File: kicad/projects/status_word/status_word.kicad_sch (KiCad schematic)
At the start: 9 parts, among them J1 peripheral_addr_bus_connector, J2 peripheral_aux_connector, J3 peripheral_membank_connector

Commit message: WIP on status word
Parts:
- added C2, C3, C4, C5, C6, C7: C, Capacitor_THT:C_Disc_D5.0mm_W2.5mm_P5.00mm, symbol Device:C
- added D1, D10, D11, D12, D13, D14, D15, D16, D2, D3, D4, D5, D6, D7, D8, D9: LED, sixteen-bit-computer:LED_D5.0mm_Horizontal_O3.81mm_Z3.0mm, symbol Device:LED
- added J10, J11, J12, J13, J6, J7, J8, J9: Conn_01x02_Pin, Connector_PinHeader_2.54mm:PinHeader_1x02_P2.54mm_Vertical, symbol Connector:Conn_01x02_Pin
- added J14: Conn_01x08_Socket, Connector_PinSocket_2.54mm:PinSocket_1x08_P2.54mm_Horizontal, symbol Connector:Conn_01x08_Socket
- added J4: Conn_01x16_Socket, Connector_PinSocket_2.54mm:PinSocket_1x16_P2.54mm_Horizontal, symbol Connector:Conn_01x16_Socket
- added J5: Conn_01x04_Socket, Connector_PinSocket_2.54mm:PinSocket_1x04_P2.54mm_Horizontal, symbol Connector:Conn_01x04_Socket
- added RN1, RN2, RN3: R_Network08_US, Resistor_THT:R_Array_SIP9, symbol Device:R_Network08_US
- added U1: 74HC10, Package_DIP:DIP-14_W7.62mm_Socket, symbol sixteen-bit-computer:74HC10
- added U2, U3: 74HC377, Package_DIP:DIP-20_W7.62mm_Socket, symbol sixteen-bit-computer:74HC377
- added U4, U5, U6, U7: 74HC245, Package_DIP:DIP-20_W7.62mm_Socket, symbol sixteen-bit-computer:74HC245
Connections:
- net RFM renamed MEM_ACT
- net WTM renamed ~{RFM}/WTM
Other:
- moved on the sheet: C1, J2

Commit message: Status word schematic complete - WIP on PCB.
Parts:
- removed TP1: TestPoint, Connector_Pin:Pin_D1.0mm_L10.0mm, symbol Connector:TestPoint
- added J15: Conn_01x03_Pin, symbol Connector:Conn_01x03_Pin
- added R2, R3, R4: 10K, Resistor_THT:R_Axial_DIN0207_L6.3mm_D2.5mm_P10.16mm_Horizontal, symbol Device:R_US
- R1: value R_US -> 10K
- RN1, RN2: value R_Network08_US -> 2K
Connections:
- net DATA_BUS_00: now also U3.3 (D0), U4.2 (A1)
- net DATA_BUS_01: now also U3.4 (D1), U4.4 (A3)
- net DATA_BUS_02: now also U3.7 (D2), U4.6 (A5)
- net DATA_BUS_03: now also U3.8 (D3), U4.8 (A7)
- net DATA_BUS_04: now also U3.13 (D4), U4.9 (A8)
- net DATA_BUS_05: now also U3.14 (D5), U4.7 (A6)
- net DATA_BUS_06: now also U3.17 (D6), U4.5 (A4)
- net DATA_BUS_07: now also U3.18 (D7), U4.3 (A2)
- net DATA_BUS_08: now also U2.3 (D0), U5.2 (A1)
- net DATA_BUS_09: now also U2.4 (D1), U5.3 (A2)
- net DATA_BUS_10: now also U2.7 (D2), U5.4 (A3)
- net DATA_BUS_11: now also U2.8 (D3), U5.5 (A4)
- net DATA_BUS_12: now also U2.13 (D4), U5.6 (A5)
- net DATA_BUS_13: now also U2.14 (D5), U5.7 (A6)
- net DATA_BUS_14: now also U2.17 (D6), U5.8 (A7)
- net DATA_BUS_15: now also U2.18 (D7), U5.9 (A8)
- net DATA_CLK: now also U2.11 (CP), U3.11 (CP)
- net GND: now also C1.2, C2.1, C3.1, C4.1, C5.1, C6.1, C7.1, J10.1 (Pin_1), J10.2 (Pin_2), J12.1 (Pin_1), J12.2 (Pin_2), J6.1 (Pin_1), J6.2 (Pin_2), J8.1 (Pin_1), J8.2 (Pin_2), R1.1, RN1.1 (common), RN2.1 (common), RN3.1 (common), U1.7 (GND), U2.10 (GND), U3.10 (GND), U4.10 (GND), U5.10 (GND), U6.10 (GND), U7.10 (GND), J15.3 (Pin_3), R4.2
- net MEM_ACT: now also U1.1, U1.3
- net VCC: now also C1.1, C2.2, C3.2, C4.2, C5.2, C6.2, C7.2, U1.14 (VCC), U2.20 (VCC), U3.20 (VCC), U4.20 (VCC), U5.20 (VCC), U6.1 (DIR), U6.20 (VCC), U7.1 (DIR), U7.20 (VCC), J15.1 (Pin_1), R2.1, R3.1
- net ~{RFM}/WTM: now also U1.10, U1.11, U1.13, U1.9
- net at D3.1 (K): now also RN2.4 (R3)
- net at D3.2 (A): now also U7.13 (B6)
- net at D12.1 (K): now also RN1.5 (R4)
- net at D12.2 (A): now also U6.14 (B5)
- net at RN1.2 (R1): now also D9.1 (K)
- net at RN1.3 (R2): now also D10.1 (K)
- net at RN1.4 (R3): now also D11.1 (K)
- net at RN1.6 (R5): now also D13.1 (K)
- net at RN1.7 (R6): now also D14.1 (K)
- net at RN1.8 (R7): now also D15.1 (K)
- net at RN1.9 (R8): now also D16.1 (K)
- net at D15.2 (A): now also U6.17 (B2)
- net at D11.2 (A): now also U6.13 (B6)
- net CONTENT_13: now reaches J9.1 (Pin_1)
- net CONTENT_13: now also J4.14 (Pin_14), J9.2 (Pin_2), U2.15 (Q5), U6.4 (A3)
- net at D14.2 (A): now also U6.16 (B3)
- net at D5.1 (K): now also RN2.6 (R5)
- net at D5.2 (A): now also U7.15 (B4)
- net at D10.2 (A): now also U6.12 (B7)
- net CONTENT_14: now reaches J11.1 (Pin_1)
- net CONTENT_14: now also J11.2 (Pin_2), J4.15 (Pin_15), U2.16 (Q6), U6.3 (A2)
- net EXT_7: now reaches J14.1 (Pin_1)
- net EXT_7: now also RN3.9 (R8), U5.18 (B1)
- net EXT_6: now reaches J14.2 (Pin_2)
- net EXT_6: now also RN3.8 (R7), U5.17 (B2)
- net EXT_5: now reaches J14.3 (Pin_3)
- net EXT_5: now also RN3.7 (R6), U5.16 (B3)
- net EXT_4: now reaches J14.4 (Pin_4)
- net EXT_4: now also RN3.6 (R5), U5.15 (B4)
- net EXT_3: now reaches J14.5 (Pin_5)
- net EXT_3: now also RN3.5 (R4), U5.14 (B5)
- net EXT_2: now reaches J14.6 (Pin_6)
- net EXT_2: now also RN3.4 (R3), U5.13 (B6)
- net EXT_1: now reaches J14.7 (Pin_7)
- net EXT_1: now also RN3.3 (R2), U5.12 (B7)
- net EXT_0: now reaches J14.8 (Pin_8)
- net EXT_0: now also RN3.2 (R1), U5.11 (B8)
- net at D6.1 (K): now also RN2.7 (R6)
- net at D6.2 (A): now also U7.16 (B3)
- net CONTENT_15: now reaches J13.1 (Pin_1)
- net CONTENT_15: now also J13.2 (Pin_2), J4.16 (Pin_16), U2.19 (Q7), U6.2 (A1)
- net ADDRESSED: now reaches J5.1 (Pin_1)
- net ADDRESSED: now also J5.2 (Pin_2), J5.3 (Pin_3), J5.4 (Pin_4), U1.2, U1.4, R4.1
- net ~{WTM}: now reaches U2.1 (~{E})
- net ~{WTM}: now also U1.12, U3.1 (~{E})
- net CONTENT_12: now reaches U2.12 (Q4)
- net CONTENT_12: now also J4.13 (Pin_13), J7.1 (Pin_1), J7.2 (Pin_2), U6.5 (A4)
- net CONTENT_08: now reaches U2.2 (Q0)
- net CONTENT_08: now also J4.9 (Pin_9), U6.9 (A8)
- net CONTENT_09: now reaches U2.5 (Q1)
- net CONTENT_09: now also J4.10 (Pin_10), U6.8 (A7)
- net CONTENT_10: now reaches U2.6 (Q2)
- net CONTENT_10: now also J4.11 (Pin_11), U6.7 (A6)
- net CONTENT_11: now reaches U2.9 (Q3)
- net CONTENT_11: now also J4.12 (Pin_12), U6.6 (A5)
- net at D4.1 (K): now also RN2.5 (R4)
- net at D4.2 (A): now also U7.14 (B5)
- net at D7.1 (K): now also RN2.8 (R7)
- net at D7.2 (A): now also U7.17 (B2)
- net RFM/~{WTM}: now reaches U1.8
- net RFM/~{WTM}: now also U1.5
- net at U6.11 (B8): now also D9.2 (A)
- net at U6.15 (B4): now also D13.2 (A)
- net at U6.18 (B1): now also D16.2 (A)
- net LED_~{OE}: now reaches U6.19 (~{OE})
- net LED_~{OE}: now also R1.2, U7.19 (~{OE}), J15.2 (Pin_2)
- net CONTENT_04: now reaches U3.12 (Q4)
- net CONTENT_04: now also J4.5 (Pin_5), U4.11 (B8), U7.5 (A4)
- net CONTENT_05: now reaches U3.15 (Q5)
- net CONTENT_05: now also J4.6 (Pin_6), U4.13 (B6), U7.4 (A3)
- net CONTENT_06: now reaches U3.16 (Q6)
- net CONTENT_06: now also J4.7 (Pin_7), U4.15 (B4), U7.3 (A2)
- net CONTENT_07: now reaches U3.19 (Q7)
- net CONTENT_07: now also J4.8 (Pin_8), U4.17 (B2), U7.2 (A1)
- net CONTENT_00: now reaches U3.2 (Q0)
- net CONTENT_00: now also J4.1 (Pin_1), U4.18 (B1), U7.9 (A8)
- net CONTENT_01: now reaches U3.5 (Q1)
- net CONTENT_01: now also J4.2 (Pin_2), U4.16 (B3), U7.8 (A7)
- net CONTENT_02: now reaches U3.6 (Q2)
- net CONTENT_02: now also J4.3 (Pin_3), U4.14 (B5), U7.7 (A6)
- net CONTENT_03: now reaches U3.9 (Q3)
- net CONTENT_03: now also J4.4 (Pin_4), U4.12 (B7), U7.6 (A5)
- net ~{RFM}: now reaches U1.6
- net ~{RFM}: now also U4.19 (~{OE}), U5.19 (~{OE}), R2.2, R3.2
- net at RN2.2 (R1): now also D1.1 (K)
- net at RN2.3 (R2): now also D2.1 (K)
- net at RN2.9 (R8): now also D8.1 (K)
- net at D2.2 (A): now also U7.12 (B7)
- net at D1.2 (A): now also U7.11 (B8)
- net at D8.2 (A): now also U7.18 (B1)
- net ADDR_BUS_00: no longer names the net of J1.17 (A_00)
- net ADDR_BUS_01: no longer names the net of J1.18 (A_01)
- net ADDR_BUS_02: no longer names the net of J1.19 (A_02)
- net ADDR_BUS_03: no longer names the net of J1.20 (A_03)
- net ADDR_BUS_04: no longer names the net of J1.21 (A_04)
- net ADDR_BUS_05: no longer names the net of J1.22 (A_05)
- net ADDR_BUS_06: no longer names the net of J1.23 (A_06)
- net ADDR_BUS_07: no longer names the net of J1.24 (A_07)
- net ADDR_BUS_08: no longer names the net of J1.25 (A_08)
- net ADDR_BUS_09: no longer names the net of J1.26 (A_09)
- net ADDR_BUS_10: no longer names the net of J1.27 (A_10)
- net ADDR_BUS_11: no longer names the net of J1.28 (A_11)
- net ADDR_BUS_12: no longer names the net of J1.29 (A_12)
- net ADDR_BUS_13: no longer names the net of J1.30 (A_13)
- net ADDR_BUS_14: no longer names the net of J1.31 (A_14)
- net ADDR_BUS_15: no longer names the net of J1.32 (A_15)
- net BANK_BUS_00: no longer names the net of J3.1 (B_00)
- net BANK_BUS_01: no longer names the net of J3.2 (B_01)
- net BANK_BUS_02: no longer names the net of J3.3 (B_02)
- net BANK_BUS_03: no longer names the net of J3.4 (B_03)
- net BANK_BUS_04: no longer names the net of J3.5 (B_04)
- net BANK_BUS_05: no longer names the net of J3.6 (B_05)
- net BANK_BUS_06: no longer names the net of J3.7 (B_06)
- net BANK_BUS_07: no longer names the net of J3.8 (B_07)
- net BANK_BUS_08: no longer names the net of J3.9 (B_08)
- net BANK_BUS_09: no longer names the net of J3.10 (B_09)
- net BANK_BUS_10: no longer names the net of J3.11 (B_10)
- net BANK_BUS_11: no longer names the net of J3.12 (B_11)
- net BANK_BUS_12: no longer names the net of J3.13 (B_12)
- net BANK_BUS_13: no longer names the net of J3.14 (B_13)
- net BANK_BUS_14: no longer names the net of J3.15 (B_14)
- net BANK_BUS_15: no longer names the net of J3.16 (B_15)
- net CTL_CLK: no longer names the net of J2.8 (CCLK)
- net RESET: no longer names the net of J2.14 (RST)
- no-connect marks 0 -> 34
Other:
- note added: "Content inpupt and output"
- note added: "Control signal decode"
- note added: "LED Output"
- moved on the sheet: C1, C2, C3, C4, C5, C6, C7, C97, C98, C99, D1, D10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

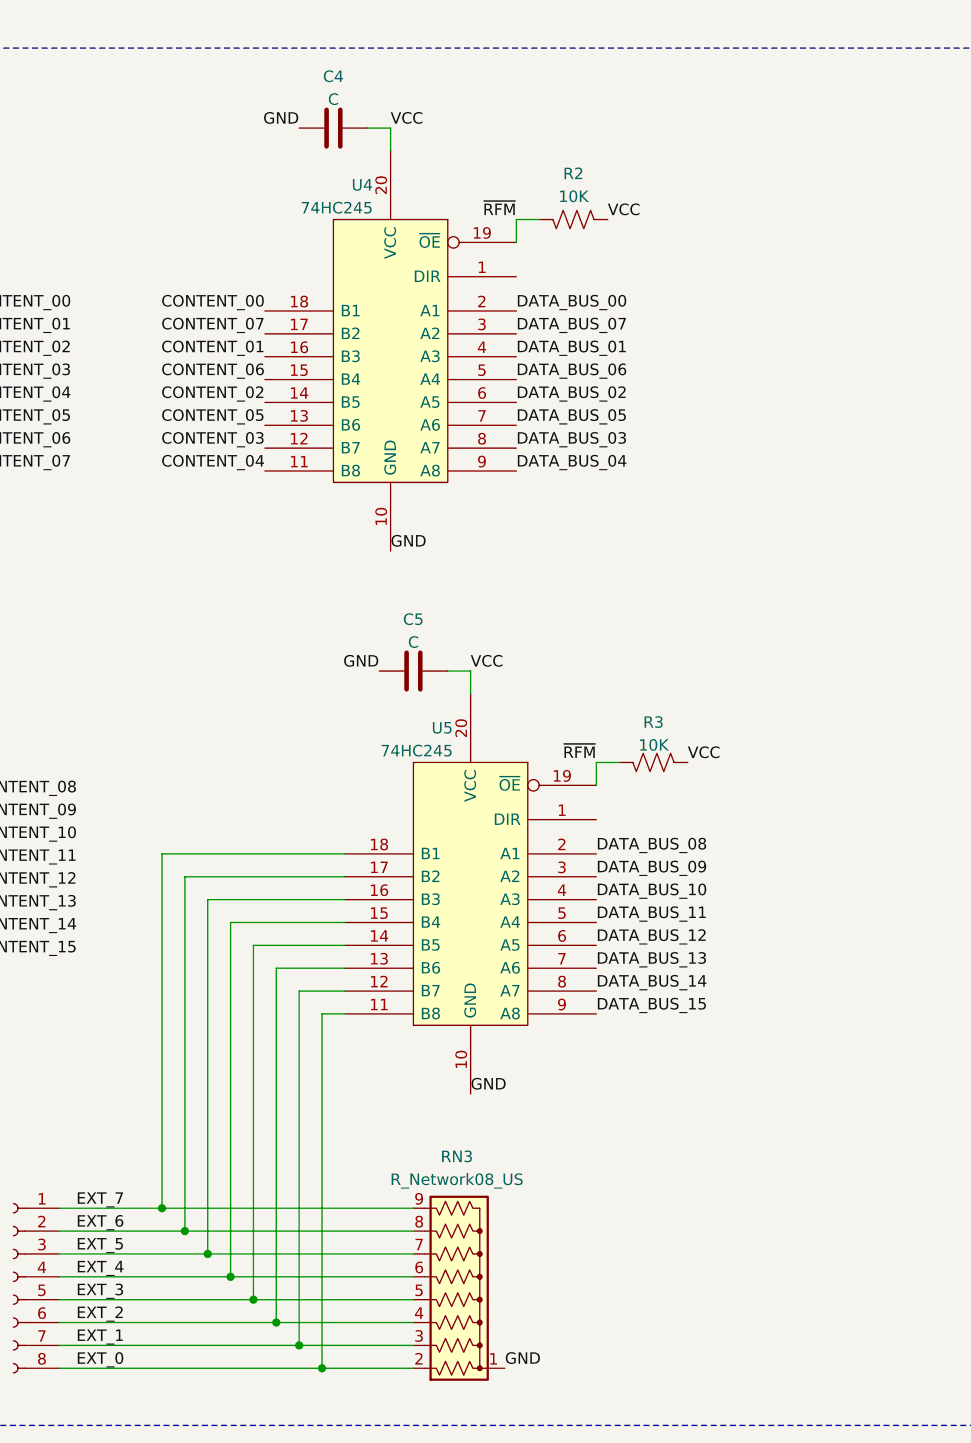
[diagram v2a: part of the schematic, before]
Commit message: WIP on status word PCB
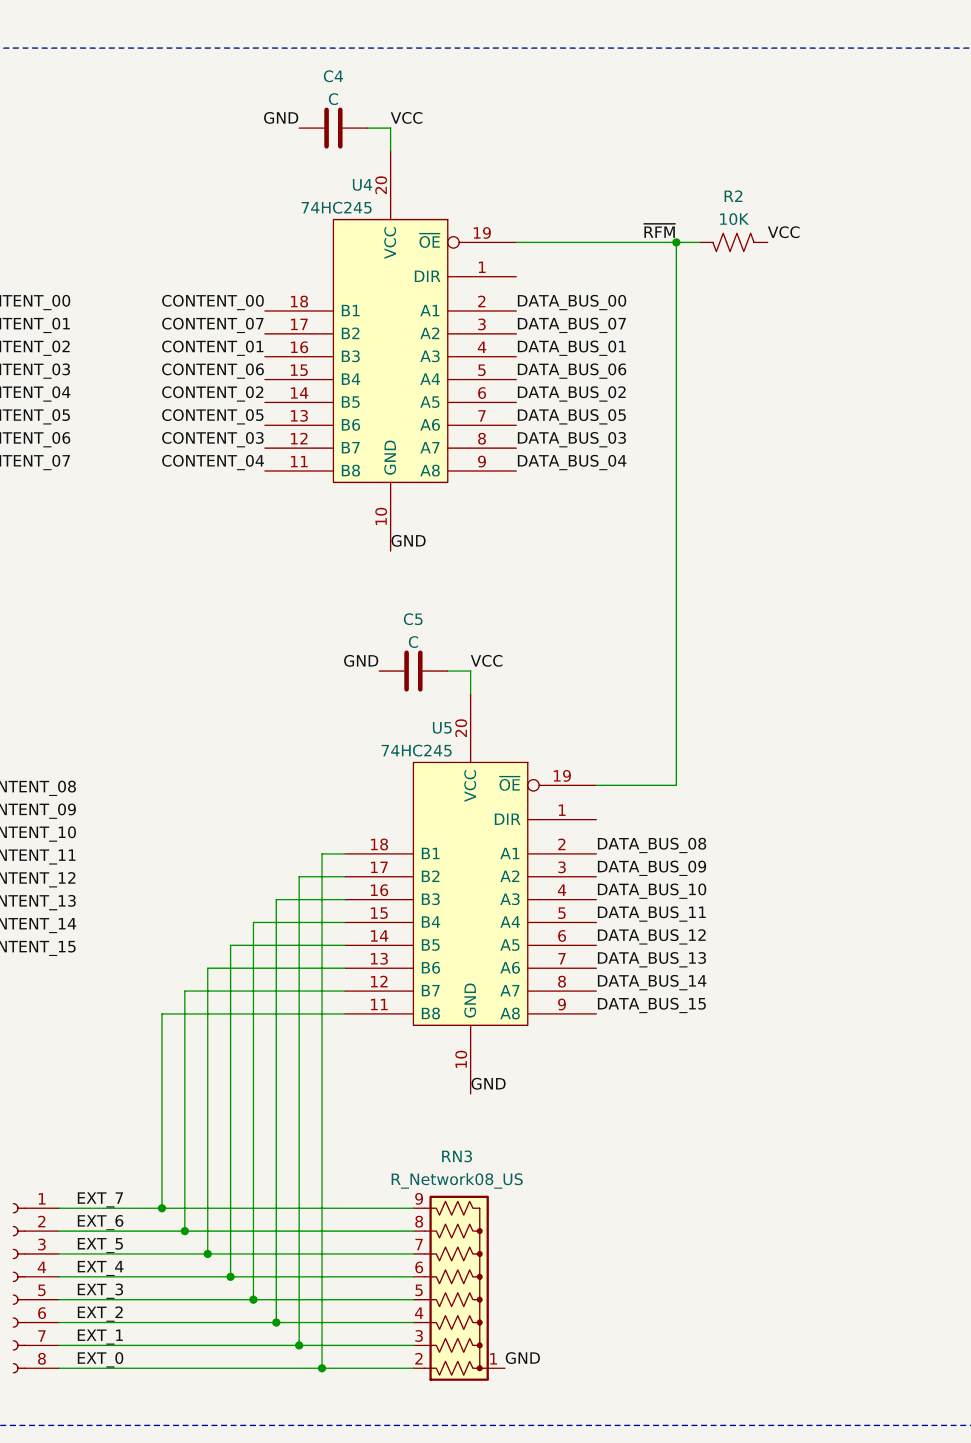
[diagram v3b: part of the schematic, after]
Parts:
- removed R3: 10K, Resistor_THT:R_Axial_DIN0207_L6.3mm_D2.5mm_P10.16mm_Horizontal, symbol Device:R_US
- J15: footprint (none) -> Connector_PinHeader_2.54mm:PinHeader_1x03_P2.54mm_Horizontal
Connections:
- net EXT_0: now also U5.18 (B1); no longer U5.11 (B8)
- net EXT_1: now also U5.17 (B2); no longer U5.12 (B7)
- net EXT_2: now also U5.16 (B3); no longer U5.13 (B6)
- net EXT_3: now also U5.15 (B4); no longer U5.14 (B5)
- net EXT_4: now also U5.14 (B5); no longer U5.15 (B4)
- net EXT_5: now also U5.13 (B6); no longer U5.16 (B3)
- net EXT_6: now also U5.12 (B7); no longer U5.17 (B2)
- net EXT_7: now also U5.11 (B8); no longer U5.18 (B1)
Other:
- moved on the sheet: R2
